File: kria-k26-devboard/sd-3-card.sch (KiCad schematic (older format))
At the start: 13 parts, among them U23 NVT4858HKZ

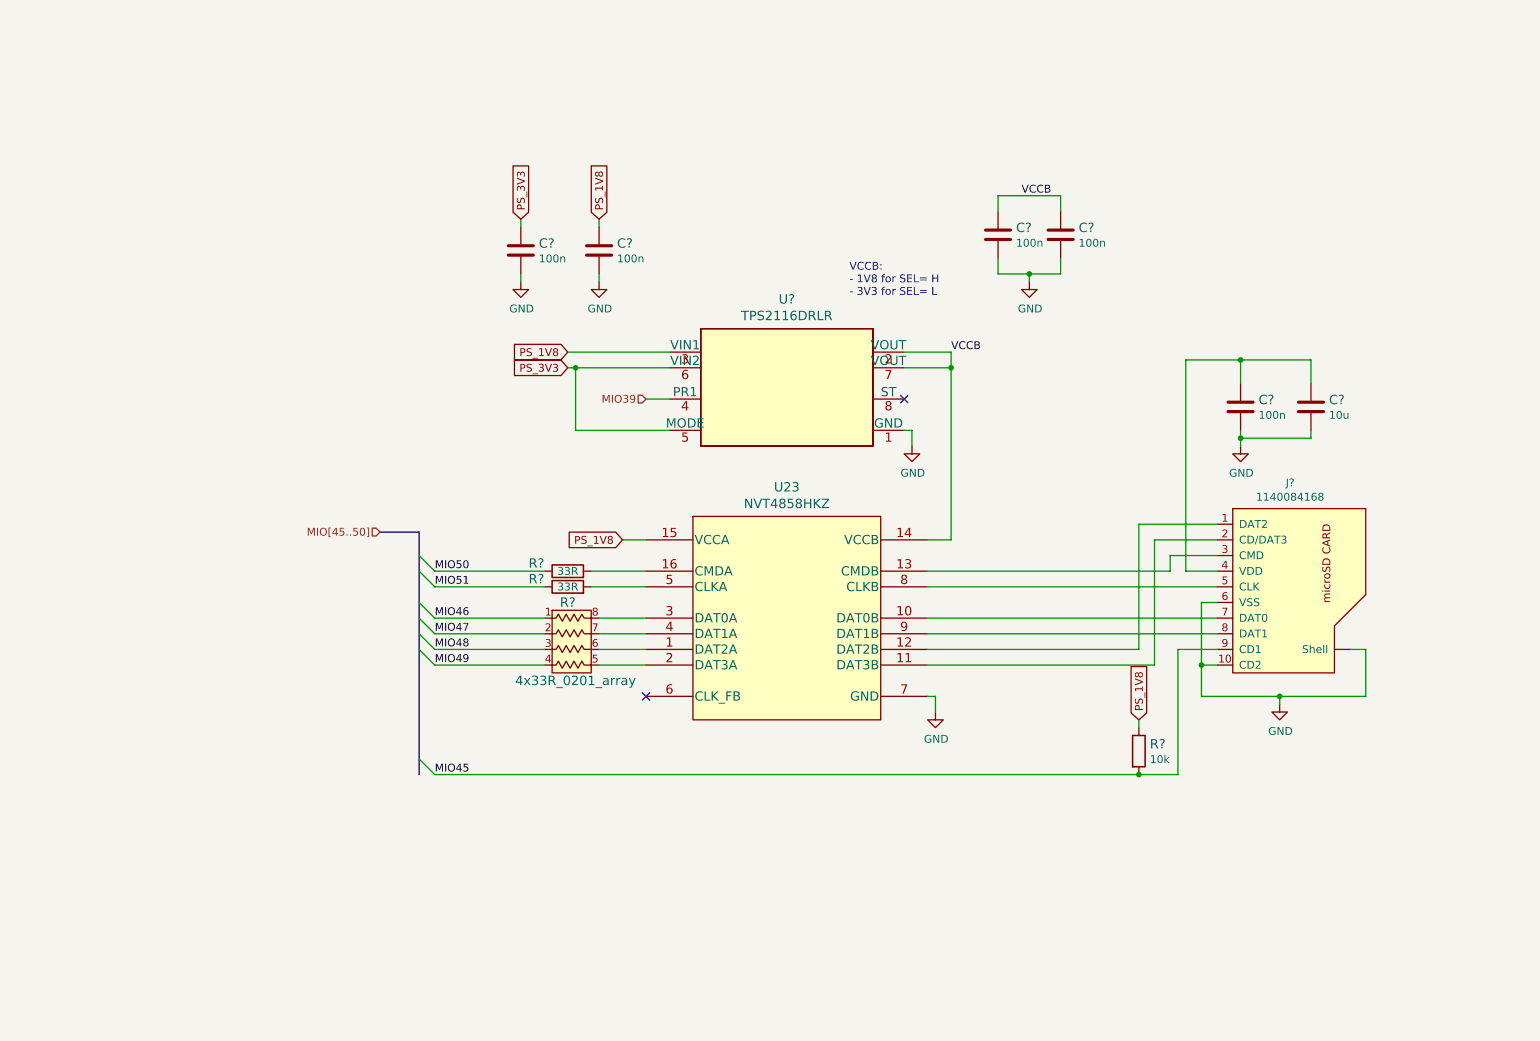
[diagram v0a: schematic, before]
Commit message: Finished reset logic, added crystal gen. to USB PHY, create power toggle for SD 3.0
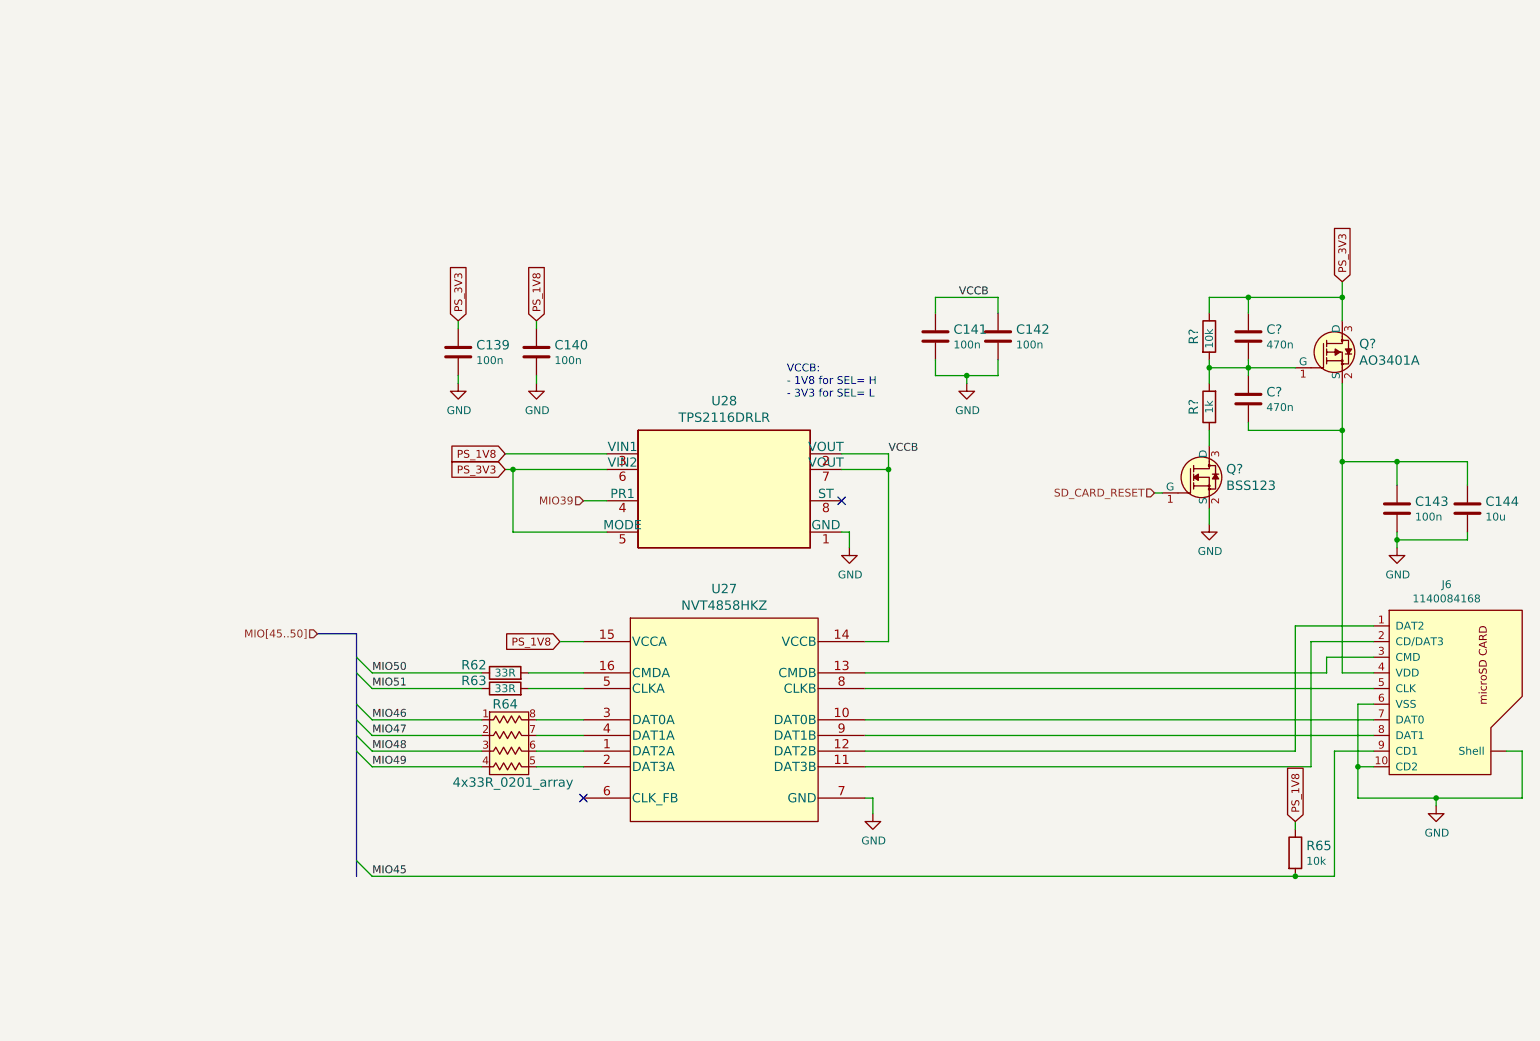
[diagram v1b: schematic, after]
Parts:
- added C? (x2): C_470n_0402, antmicro-footprints:0402-cap, symbol antmicroCapacitors0402:C_470n_0402
- added Q?: AO3401A, antmicro-footprints:SOT-23-3, symbol antmicroTransistorsFETsMOSFETsSingle:AO3401A
- added Q?: BSS123, antmicro-footprints:SOT-23-3, symbol antmicroTransistorsFETsMOSFETsSingle:BSS123
- added R?: R_1k_0402, antmicro-footprints:0402-res, symbol antmicroResistors0402:R_1k_0402
- added R?: R_10k_0402, antmicro-footprints:0402-res, symbol antmicroResistors0402:R_10k_0402
- gave numbers to parts that had none: 12
- renumbered U23 to U27
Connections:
- net GND: now also Q?.2 (S)
- net PS_3V3: now also C?.1, Q?.3 (D), R?.1
- net at C143.1, C144.1, J6.4 (VDD): now also C?.2, Q?.2 (S)
- new net: Q?.3 (D), R?.1
- new net: C?.1, C?.2, Q?.1 (G), R?.2, R?.2
- new net SD_CARD_RESET: Q?.1 (G)
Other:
- moved on the sheet: C139, C140, C141, C142, C143, C144, J6, R62, R63, R64, R65, U27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

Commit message: Progress on Debug sheet
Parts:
- gave numbers to parts that had none: 6
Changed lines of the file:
@@
 Connection ~ 8800 6100
 $Comp
-L antmicroTransistorsFETsMOSFETsSingle:AO3401A Q?
+L antmicroTransistorsFETsMOSFETsSingle:AO3401A Q4
 U 1 1 6678C047
 P 9100 2750
-F 0 "Q?" H 9208 2803 60  0000 L CNN
+F 0 "Q4" H 9208 2803 60  0000 L CNN
 F 1 "AO3401A" H 9208 2697 60  0000 L CNN
 F 2 "antmicro-footprints:SOT-23-3" H 9300 2950 60  0001 L CNN
@@
 $EndComp
 $Comp
-L antmicroTransistorsFETsMOSFETsSingle:BSS123 Q?
+L antmicroTransistorsFETsMOSFETsSingle:BSS123 Q3
 U 1 1 6678D115
 P 8250 3550
-F 0 "Q?" H 8358 3603 60  0000 L CNN
+F 0 "Q3" H 8358 3603 60  0000 L CNN
 F 1 "BSS123" H 8358 3497 60  0000 L CNN
 F 2 "antmicro-footprints:SOT-23-3" H 8450 3750 60  0001 L CNN
@@
 $EndComp
 $Comp
-L power:GND #PWR?
+L power:GND #PWR0264
 U 1 1 66661087
 P 8250 3850
-F 0 "#PWR?" H 8250 3600 50  0001 C CNN
+F 0 "#PWR0264" H 8250 3600 50  0001 C CNN
 F 1 "GND" H 8255 3677 50  0000 C CNN
 F 2 "" H 8250 3850 50  0001 C CNN
@@
 	8250 2400 8250 2500
 $Comp
-L antmicroResistors0402:R_1k_0402 R?
+L antmicroResistors0402:R_1k_0402 R66
 U 1 1 66639BBE
 P 8250 3100
-F 0 "R?" H 8250 3200 60  0000 C CNN
+F 0 "R66" H 8250 3200 60  0000 C CNN
 F 1 "R_1k_0402" H 8250 2950 60  0001 C CNN
 F 2 "antmicro-footprints:0402-res" H 8450 3300 60  0001 L CNN
@@
 $EndComp
 $Comp
-L antmicroCapacitors0402:C_470n_0402 C?
+L antmicroCapacitors0402:C_470n_0402 C146
 U 1 1 666642E9
 P 8500 2650
-F 0 "C?" H 8615 2695 60  0000 L CNN
+F 0 "C146" H 8615 2695 60  0000 L CNN
 F 1 "C_470n_0402" H 8500 2500 60  0001 C CNN
 F 2 "antmicro-footprints:0402-cap" H 8700 2850 60  0001 L CNN
@@
 $EndComp
 $Comp
-L antmicroResistors0402:R_10k_0402 R?
+L antmicroResistors0402:R_10k_0402 R3
 U 1 1 6667AA59
 P 8250 2650
-F 0 "R?" H 8200 2550 60  0000 L CNN
+F 0 "R3" H 8200 2550 60  0000 L CNN
 F 1 "R_10k_0402" H 8250 2500 60  0001 C CNN
 F 2 "antmicro-footprints:0402-res" H 8450 2850 60  0001 L CNN
@@
 	9100 2550 9100 2400
 $Comp
-L antmicroCapacitors0402:C_470n_0402 C?
+L antmicroCapacitors0402:C_470n_0402 C147
 U 1 1 667B7A84
 P 8500 3050
-F 0 "C?" H 8615 3095 60  0000 L CNN
+F 0 "C147" H 8615 3095 60  0000 L CNN
 F 1 "C_470n_0402" H 8500 2900 60  0001 C CNN
 F 2 "antmicro-footprints:0402-cap" H 8700 3250 60  0001 L CNN

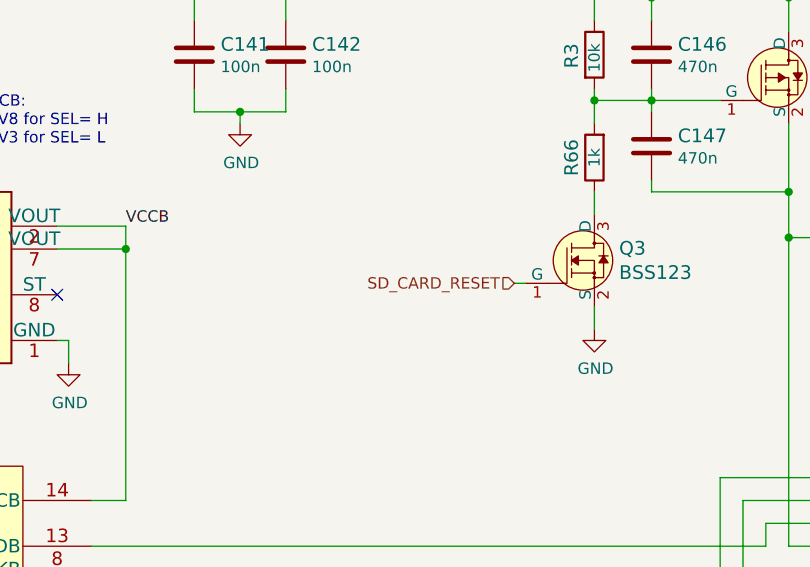
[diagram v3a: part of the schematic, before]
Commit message: Fixes on Reset pagae, progress through clock sheet
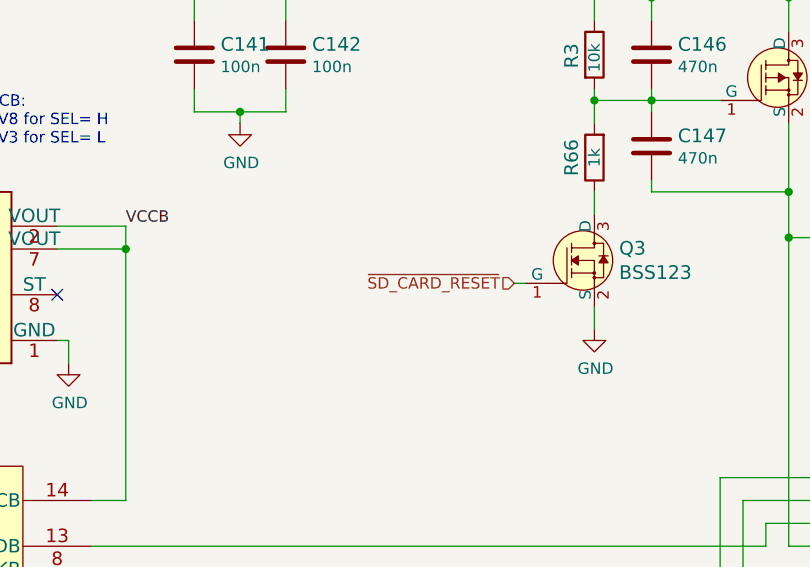
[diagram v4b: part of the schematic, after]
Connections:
- net SD_CARD_RESET renamed ~SD_CARD_RESET
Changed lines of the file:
@@
 $Descr A4 11693 8268
 encoding utf-8
-Sheet 15 19
+Sheet 12 19
 Title ""
 Date ""
@@
 	8500 2500 8500 2400
 Text HLabel 7900 3650 0    50   Input ~ 0
-SD_CARD_RESET
+~SD_CARD_RESET
 Wire Wire Line
 	9100 2550 9100 2400

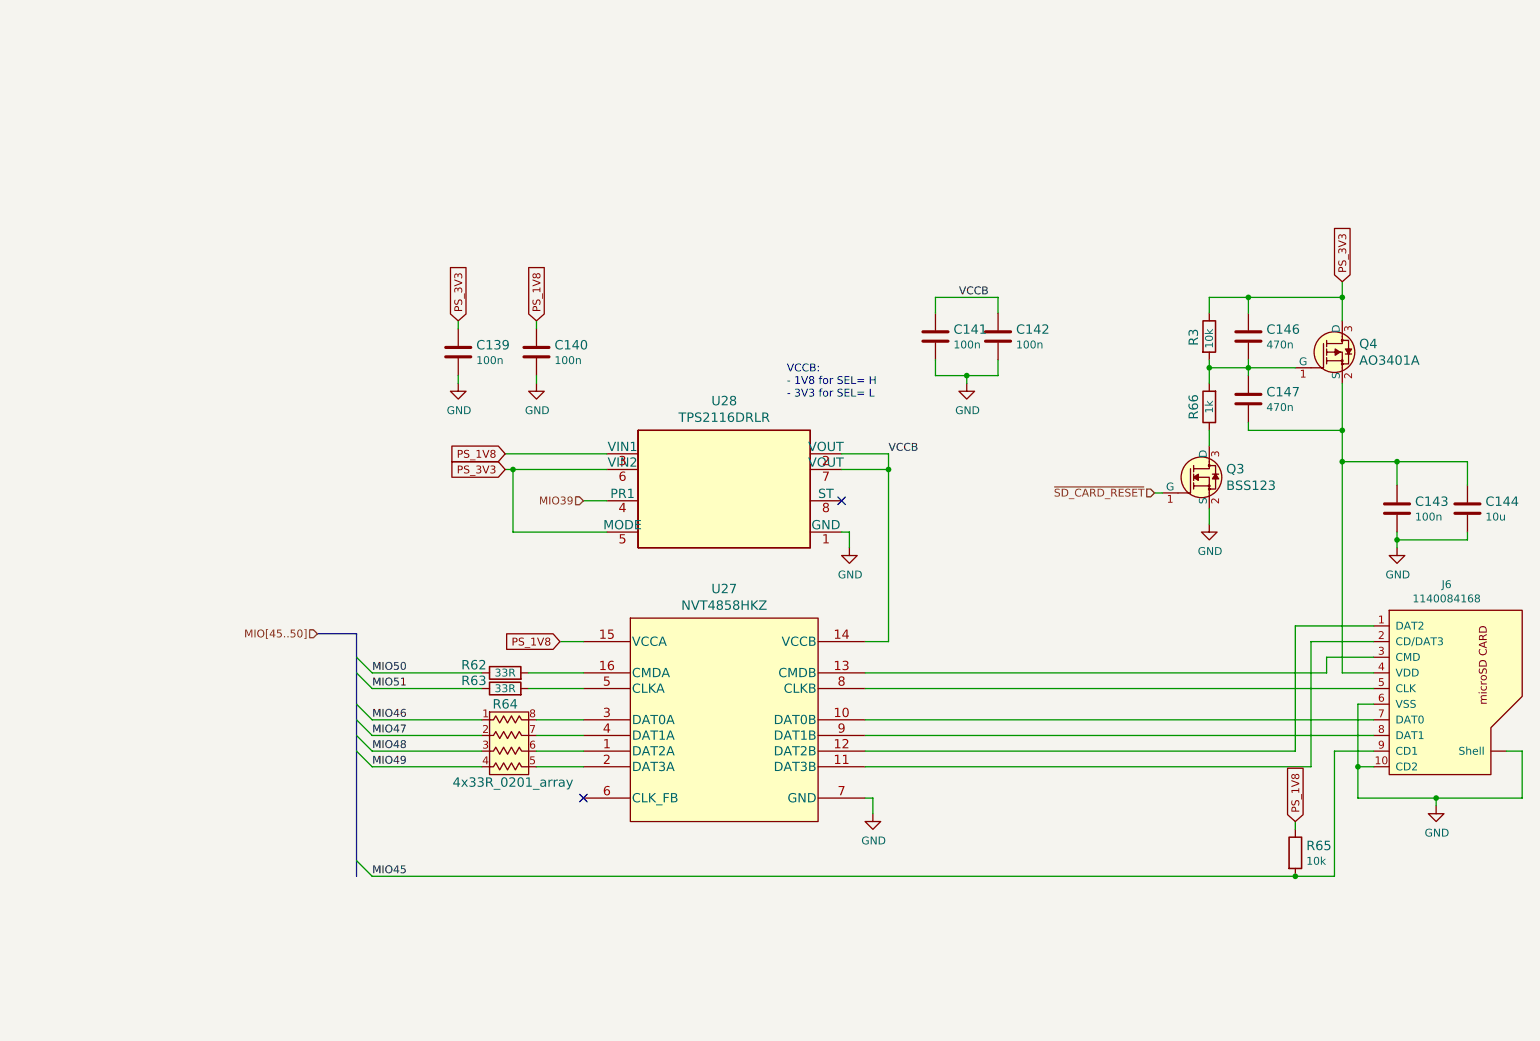
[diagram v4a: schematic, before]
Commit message: Finished tidying up the schematic
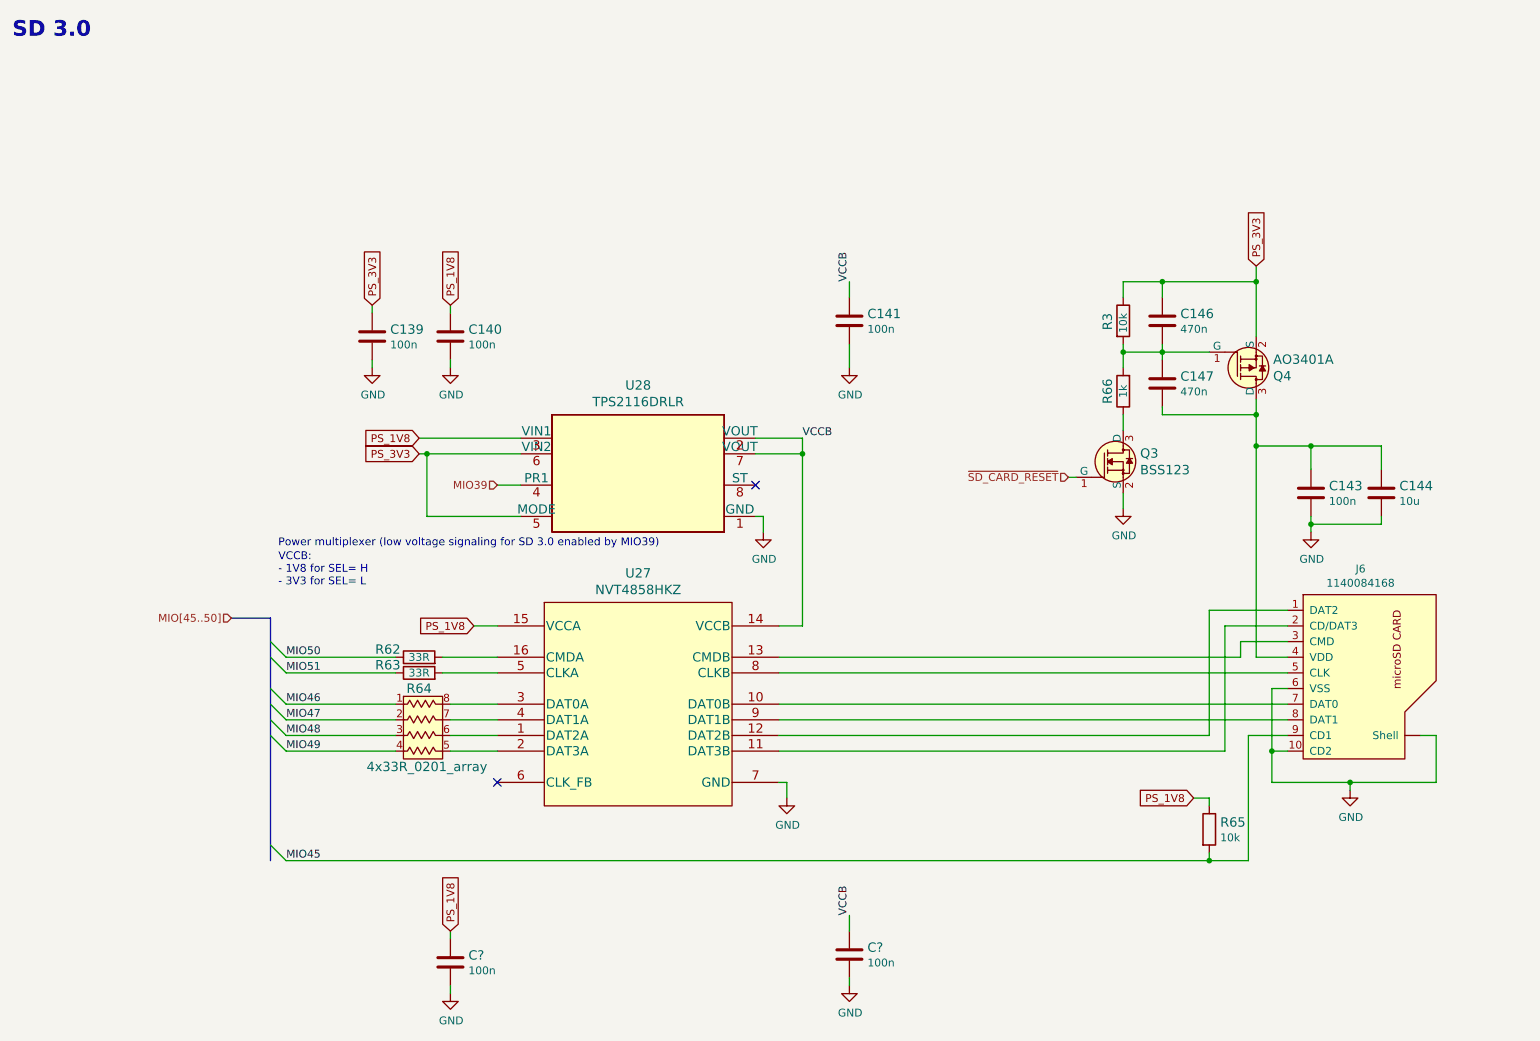
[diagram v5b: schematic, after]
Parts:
- removed C142: C_100n_0402, antmicro-footprints:0402-cap, symbol antmicroCapacitors0402:C_100n_0402
- added C? (x2): C_100n_0402, antmicro-footprints:0402-cap, symbol antmicroCapacitors0402:C_100n_0402
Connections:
- net GND: now also C?.2, C?.2
- net PS_1V8: now also C?.1
- net PS_3V3: now also Q4.2 (S); no longer Q4.3 (D)
- net VCCB: now also C?.1
- net at C143.1, C144.1, C147.2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: now also Q4.3 (D); no longer Q4.2 (S)
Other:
- note added: "Power multiplexer (low voltage signaling for SD 3.0 enabled by MIO39)"
- note added: "SD 3.0"
- moved on the sheet: C139, C140, C141, C143, C144, C146, C147, J6, Q3, Q4, R3, R62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

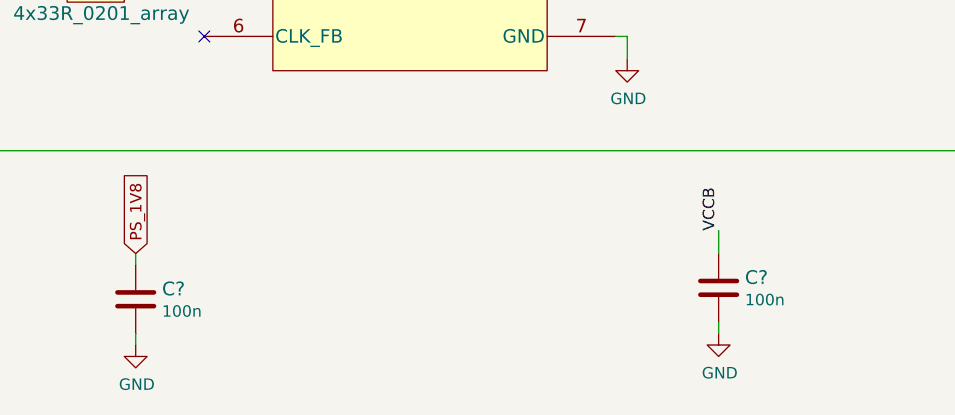
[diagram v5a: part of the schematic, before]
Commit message: Initial placement of power supply
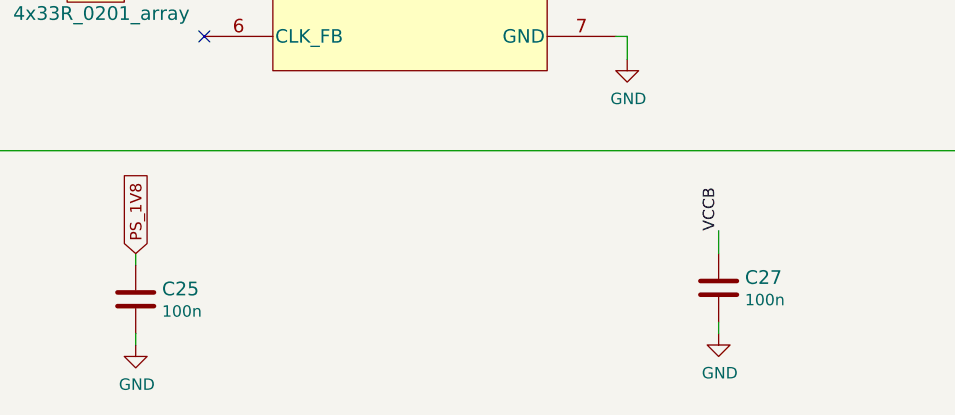
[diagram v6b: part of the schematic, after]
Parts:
- gave numbers to parts that had none: 2
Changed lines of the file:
@@
 PS_1V8
 $Comp
-L antmicroCapacitors0402:C_100n_0402 C?
+L antmicroCapacitors0402:C_100n_0402 C25
 U 1 1 6986927B
 P 3400 6650
-F 0 "C?" H 3515 6695 60  0000 L CNN
+F 0 "C25" H 3515 6695 60  0000 L CNN
 F 1 "C_100n_0402" H 3400 6500 60  0001 C CNN
 F 2 "antmicro-footprints:0402-cap" H 3600 6850 60  0001 L CNN
@@
 	3400 6850 3400 6800
 $Comp
-L power:GND #PWR?
+L power:GND #PWR0276
 U 1 1 69869287
 P 3400 6850
-F 0 "#PWR?" H 3400 6600 50  0001 C CNN
+F 0 "#PWR0276" H 3400 6600 50  0001 C CNN
 F 1 "GND" H 3405 6677 50  0000 C CNN
 F 2 "" H 3400 6850 50  0001 C CNN
@@
 $EndComp
 $Comp
-L antmicroCapacitors0402:C_100n_0402 C?
+L antmicroCapacitors0402:C_100n_0402 C27
 U 1 1 69871ED9
 P 5950 6600
-F 0 "C?" H 6065 6645 60  0000 L CNN
+F 0 "C27" H 6065 6645 60  0000 L CNN
 F 1 "C_100n_0402" H 5950 6450 60  0001 C CNN
 F 2 "antmicro-footprints:0402-cap" H 6150 6800 60  0001 L CNN
@@
 	5950 6450 5950 6350
 $Comp
-L power:GND #PWR?
+L power:GND #PWR0277
 U 1 1 6987213A
 P 5950 6800
-F 0 "#PWR?" H 5950 6550 50  0001 C CNN
+F 0 "#PWR0277" H 5950 6550 50  0001 C CNN
 F 1 "GND" H 5955 6627 50  0000 C CNN
 F 2 "" H 5950 6800 50  0001 C CNN
